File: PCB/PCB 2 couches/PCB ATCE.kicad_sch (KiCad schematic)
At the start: 28 parts, among them J1 USB_OTG, J2 Conn_Coaxial, SW1 SW_Push, SW2 SW_Push, U2 ${SIM.PARAMS}, Y1 16MHz

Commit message: Passage des fichiers KiCAD à la version 9
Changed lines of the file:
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@@
 (kicad_sch
-	(version 20231120)
+	(version 20250114)
 	(generator "eeschema")
-	(generator_version "8.0")
+	(generator_version "9.0")
 	(paper "A4")
 	(title_block
@@
 		(company "Paul ROUSSEAU")
 	)
+	(rectangle
+		(start 181.61 60.96)
+		(end 203.835 93.98)
+		(stroke
+			(width 0)
+			(type default)
+		)
+		(fill
+			(type none)
+		)
+	)
+	(rectangle
+		(start 217.805 57.15)
+		(end 247.65 90.805)
+		(stroke
+			(width 0)
+			(type default)
+		)
+		(fill
+			(type none)
+		)
+	)
+	(rectangle
+		(start 224.79 14.605)
+		(end 271.78 43.18)
+		(stroke
+			(width 0)
+			(type default)
+		)
+		(fill
+			(type none)
+		)
+	)
+	(rectangle
+		(start 63.5 62.23)
+		(end 95.25 114.3)
+		(stroke
+			(width 0)
+			(type default)
+		)
+		(fill
+			(type none)
+		)
+	)
+	(rectangle
+		(start 16.51 43.18)
+		(end 58.42 104.14)
+		(stroke
+			(width 0)
+			(type default)
+		)
+		(fill
+			(type none)
+		)
+	)
+	(text "ICP1"
+		(exclude_from_sim no)
+		(at 170.18 100.838 0)
+		(effects
+			(font
+				(size 1.27 1.27)
+			)
+		)
+	)
+	(text "Filtre"
+		(exclude_from_sim no)
+		(at 199.39 63.246 0)
+		(effects
+			(font
+				(size 1.27 1.27)
+			)
+		)
+	)
+	(text "USB"
+		(exclude_from_sim no)
+		(at 91.44 112.776 0)
+		(effects
+			(font
+				(size 1.27 1.27)
+			)
+		)
+	)
+	(text "Résonateur"
+		(exclude_from_sim no)
+		(at 52.07 45.72 0)
+		(effects
+			(font
+				(size 1.27 1.27)
+			)
+		)
+	)
+	(text "Suiveur"
+		(exclude_from_sim no)
+		(at 242.062 60.96 0)
+		(effects
+			(font
+				(size 1.27 1.27)
+			)
+		)
+	)
+	(text "OC0A"
+		(exclude_from_sim no)
+		(at 170.942 70.104 0)
+		(effects
+			(font
+				(size 1.27 1.27)
+			)
+		)
+	)
+	(text "Découplage\nalimentation"
+		(exclude_from_sim no)
+		(at 262.128 18.034 0)
+		(effects
+			(font
+				(size 1.27 1.27)
+			)
+		)
+	)
 	(junction
 		(at 252.73 73.66)
@@
 		)
 	)
-	(rectangle
-		(start 181.61 60.96)
-		(end 203.835 93.98)
-		(stroke
-			(width 0)
-			(type default)
-		)
-		(fill
-			(type none)
-		)
-	)
-	(rectangle
-		(start 217.805 57.15)
-		(end 247.65 90.805)
-		(stroke
-			(width 0)
-			(type default)
-		)
-		(fill
-			(type none)
-		)
-	)
-	(rectangle
-		(start 224.79 14.605)
-		(end 271.78 43.18)
-		(stroke
-			(width 0)
-			(type default)
-		)
-		(fill
-			(type none)
-		)
-	)
-	(rectangle
-		(start 63.5 62.23)
-		(end 95.25 114.3)
-		(stroke
-			(width 0)
-			(type default)
-		)
-		(fill
-			(type none)
-		)
-	)
-	(rectangle
-		(start 16.51 43.18)
-		(end 58.42 104.14)
-		(stroke
-			(width 0)
-			(type default)
-		)
-		(fill
-			(type none)
-		)
-	)
-	(text "ICP1"
-		(exclude_from_sim no)
-		(at 170.18 100.838 0)
-		(effects
-			(font
-				(size 1.27 1.27)
-			)
-		)
-	)
-	(text "Filtre"
-		(exclude_from_sim no)
-		(at 199.39 63.246 0)
-		(effects
-			(font
-				(size 1.27 1.27)
-			)
-		)
-	)
-	(text "USB"
-		(exclude_from_sim no)
-		(at 91.44 112.776 0)
-		(effects
-			(font
-				(size 1.27 1.27)
-			)
-		)
-	)
-	(text "Résonateur"
-		(exclude_from_sim no)
-		(at 52.07 45.72 0)
-		(effects
-			(font
-				(size 1.27 1.27)
-			)
-		)
-	)
-	(text "Suiveur"
-		(exclude_from_sim no)
-		(at 242.062 60.96 0)
-		(effects
-			(font
-				(size 1.27 1.27)
-			)
-		)
-	)
-	(text "OC0A"
-		(exclude_from_sim no)
-		(at 170.942 70.104 0)
-		(effects
-			(font
-				(size 1.27 1.27)
-			)
-		)
-	)
-	(text "Découplage\nalimentation"
-		(exclude_from_sim no)
-		(at 262.128 18.034 0)
-		(effects
-			(font
-				(size 1.27 1.27)
-			)
-		)
-	)
 	(label "D-"
 		(at 82.55 90.17 0)
@@
 		)
 	)
+	(embedded_fonts no)
 )

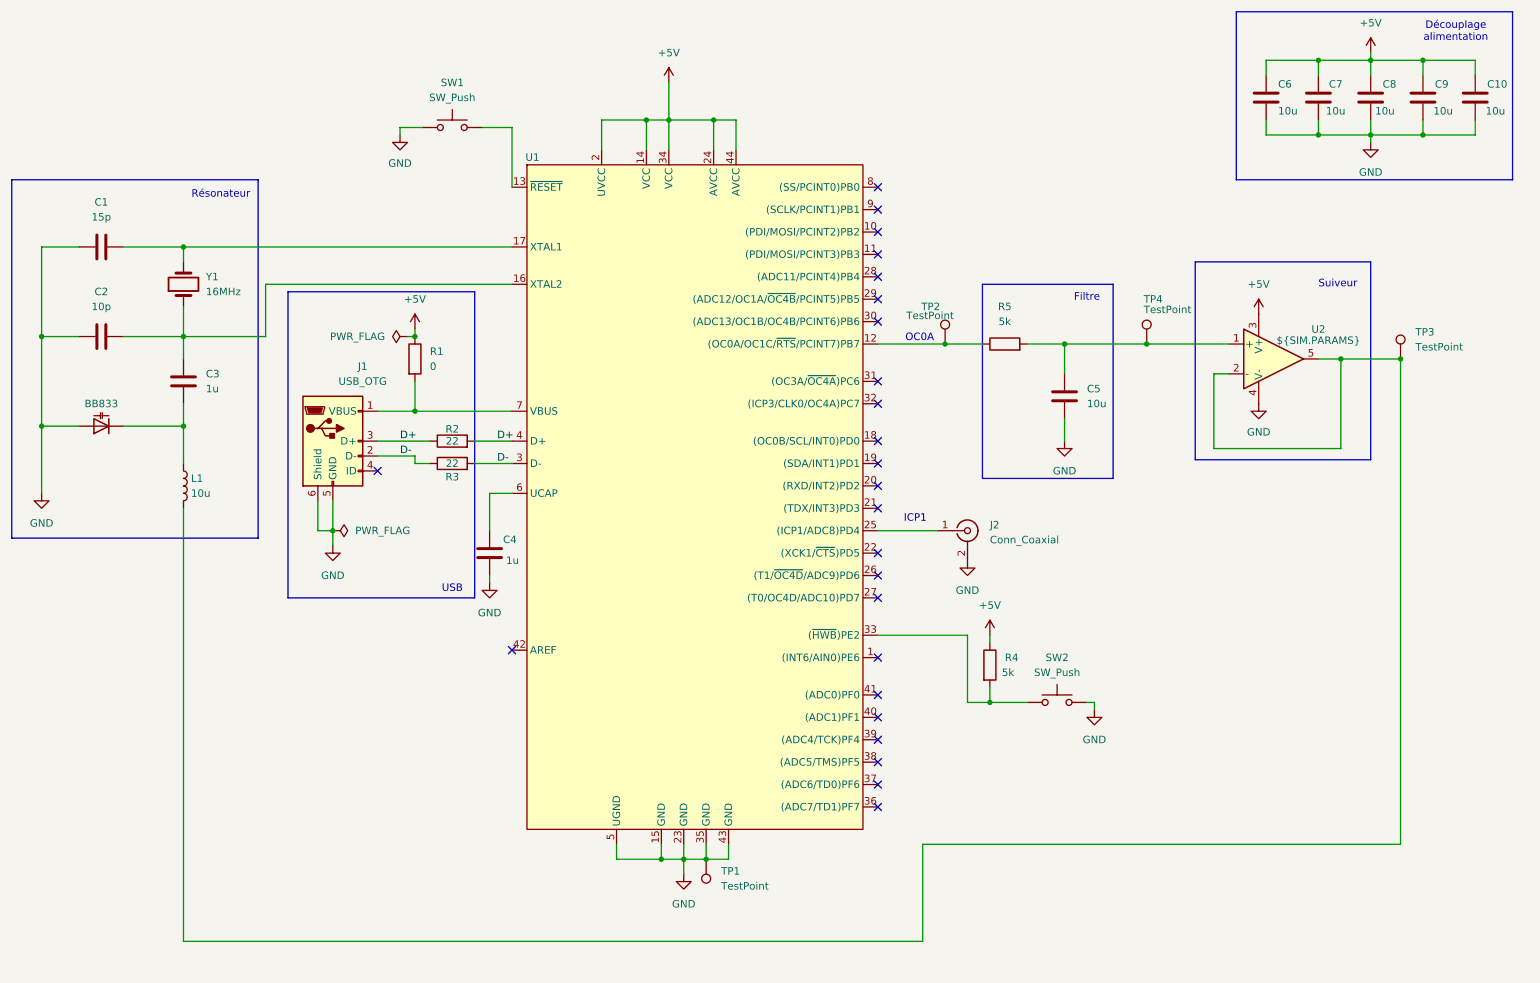
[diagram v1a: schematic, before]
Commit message: Changement des ports pour le PWM et l'ICP
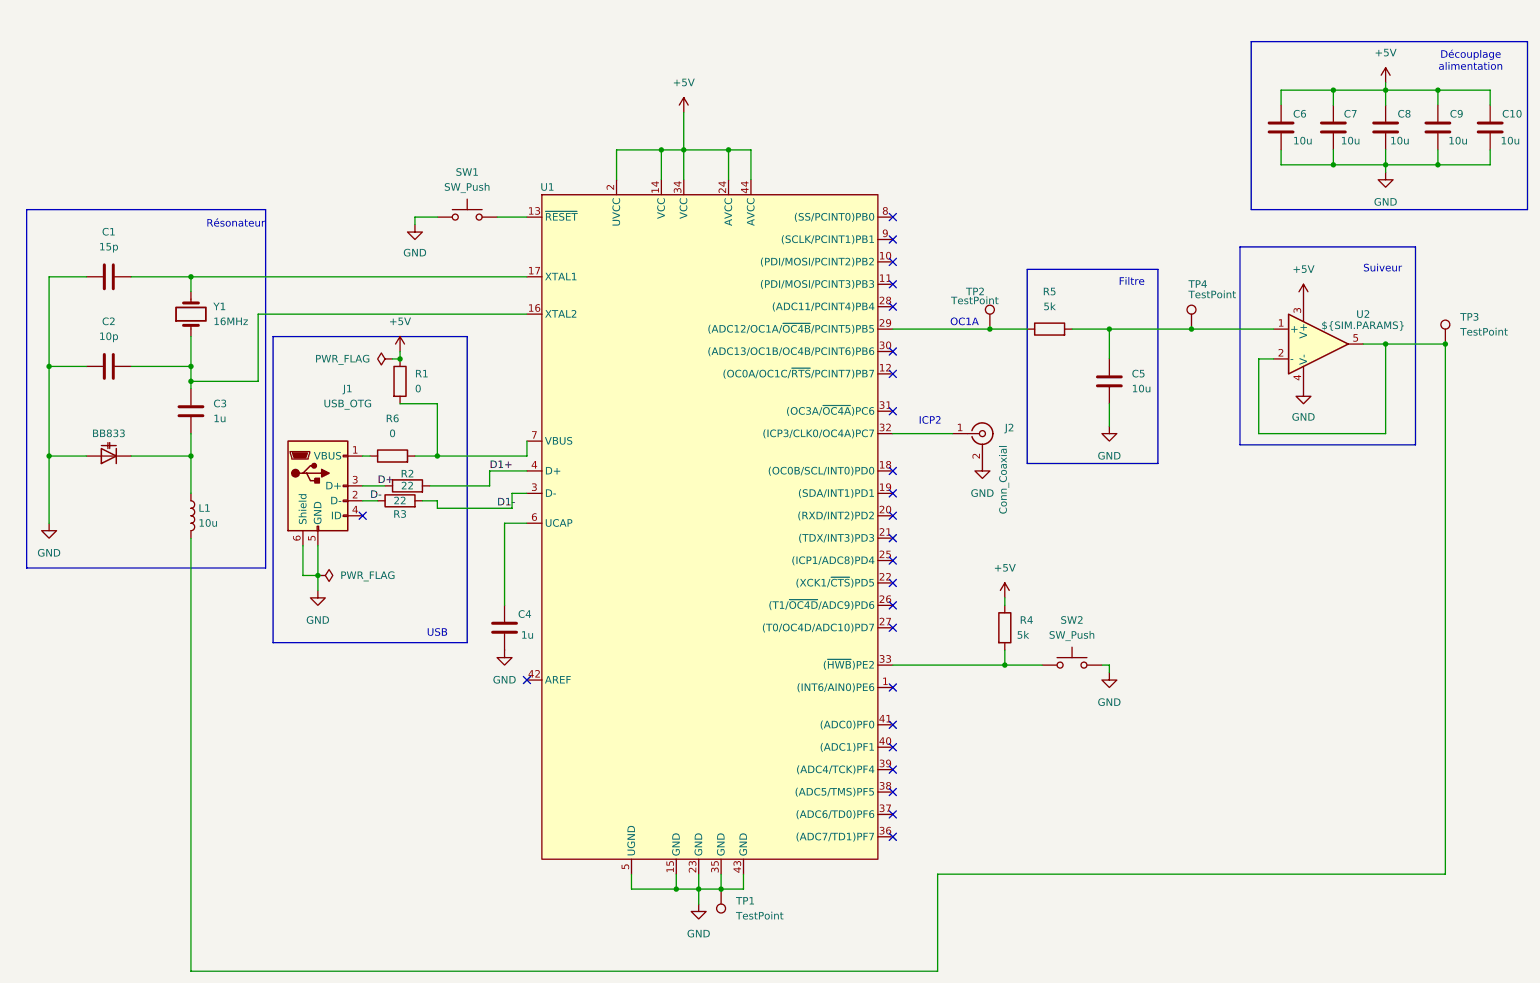
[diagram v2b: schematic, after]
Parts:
- added R6: 0, Resistor_SMD:R_0805_2012Metric_Pad1.20x1.40mm_HandSolder, symbol Device:R
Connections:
- net D+: no longer R2.2, U1.4 (D+)
- net D-: no longer R3.2, U1.3 (D-)
- net at R1.2, U1.7 (VBUS): now also R6.2; no longer J1.1 (VBUS)
- net at R5.1, TP2.1: now also U1.29 ((ADC12/OC1A/~{OC4B}/PCINT5)PB5); no longer U1.12 ((OC0A/OC1C/~{RTS}/PCINT7)PB7)
- net at U1.25 ((ICP1/ADC8)PD4): no longer J2.1 (In)
- net at U1.32 ((ICP3/CLK0/OC4A)PC7): now also J2.1 (In)
- new net: J1.1 (VBUS), R6.1
- new net D1+: R2.2, U1.4 (D+)
- new net D1-: R3.2, U1.3 (D-)
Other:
- note added: "ICP2"
- note added: "OC1A"
- note removed: "ICP1"
- note removed: "OC0A"
- moved on the sheet: BB833, C1, C10, C2, C3, C4, C5, C6, C7, C8, C9, J1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

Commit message: modification pcb (empreinte test point + routage nouveau pwm)
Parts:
- TP1, TP2, TP3, TP4: footprint TestPoint:TestPoint_Keystone_5000-5004_Miniature -> TestPoint:TestPoint_Pad_D1.5mm
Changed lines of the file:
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@@
 			)
 		)
-		(property "Footprint" "TestPoint:TestPoint_Keystone_5000-5004_Miniature"
+		(property "Footprint" "TestPoint:TestPoint_Pad_D1.5mm"
 			(at 222.25 68.58 0)
 			(effects
@@
 			)
 		)
-		(property "Footprint" "TestPoint:TestPoint_Keystone_5000-5004_Miniature"
+		(property "Footprint" "TestPoint:TestPoint_Pad_D1.5mm"
 			(at 132.08 163.83 0)
 			(effects
@@
 			)
 		)
-		(property "Footprint" "TestPoint:TestPoint_Keystone_5000-5004_Miniature"
+		(property "Footprint" "TestPoint:TestPoint_Pad_D1.5mm"
 			(at 187.96 68.58 0)
 			(effects
@@
 			)
 		)
-		(property "Footprint" "TestPoint:TestPoint_Keystone_5000-5004_Miniature"
+		(property "Footprint" "TestPoint:TestPoint_Pad_D1.5mm"
 			(at 265.43 71.12 0)
 			(effects

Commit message: Mise au propre du schéma électrique
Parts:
- removed R1: 0, Resistor_SMD:R_0805_2012Metric_Pad1.20x1.40mm_HandSolder, symbol Device:R
- C5: value 10u -> 1u
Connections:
- net +5V: now also R6.2, U1.7 (VBUS)
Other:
- note added: "ICP3"
- note removed: "ICP2"
- moved on the sheet: C10, C4, C6, C7, C8, C9, J1, R2, R3, R6
